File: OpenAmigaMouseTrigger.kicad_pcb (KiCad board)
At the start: 2 copper layers, 23.9 x 22.9 mm, 8 parts, among them J1 AMIGA_SIGNALS, J2 OUTPUT, J3 POWER, J99 OSHW_LOGO, U1 74LS74

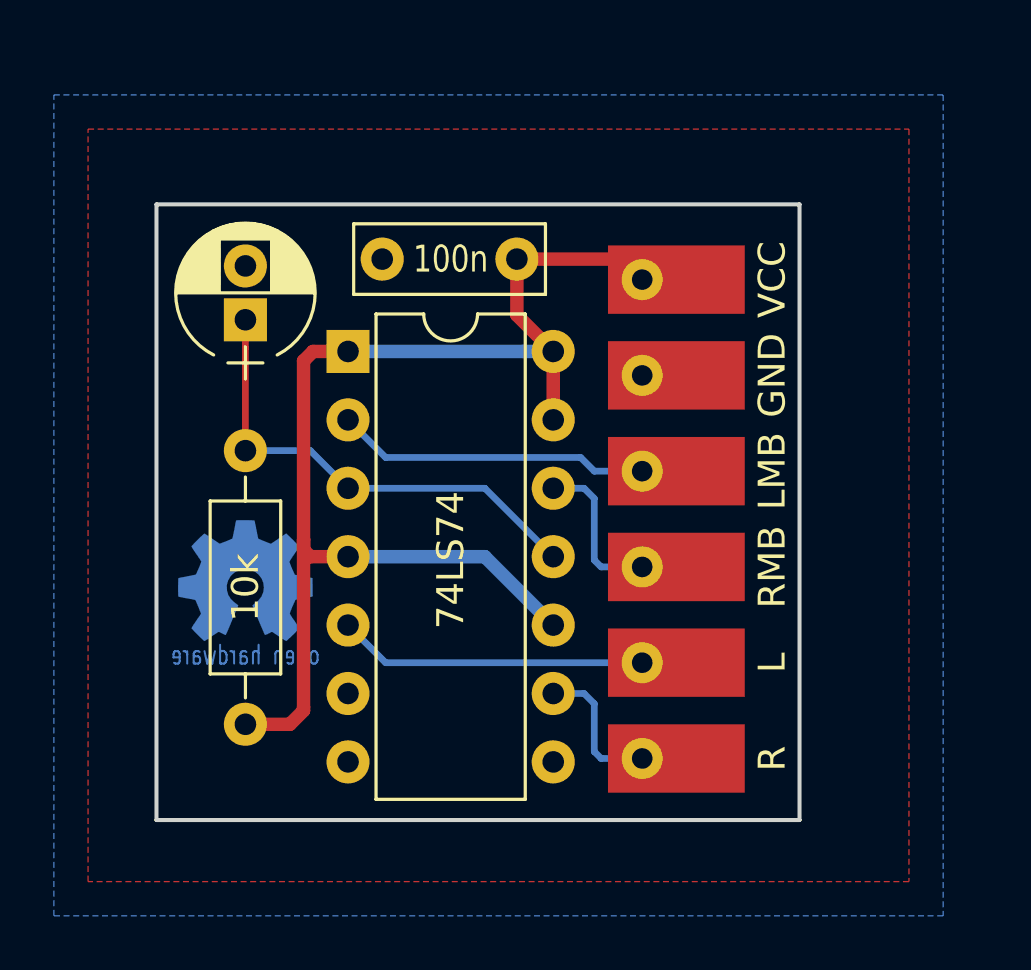
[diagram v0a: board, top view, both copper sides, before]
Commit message: Round corners, stitch grounds, routing adjustments
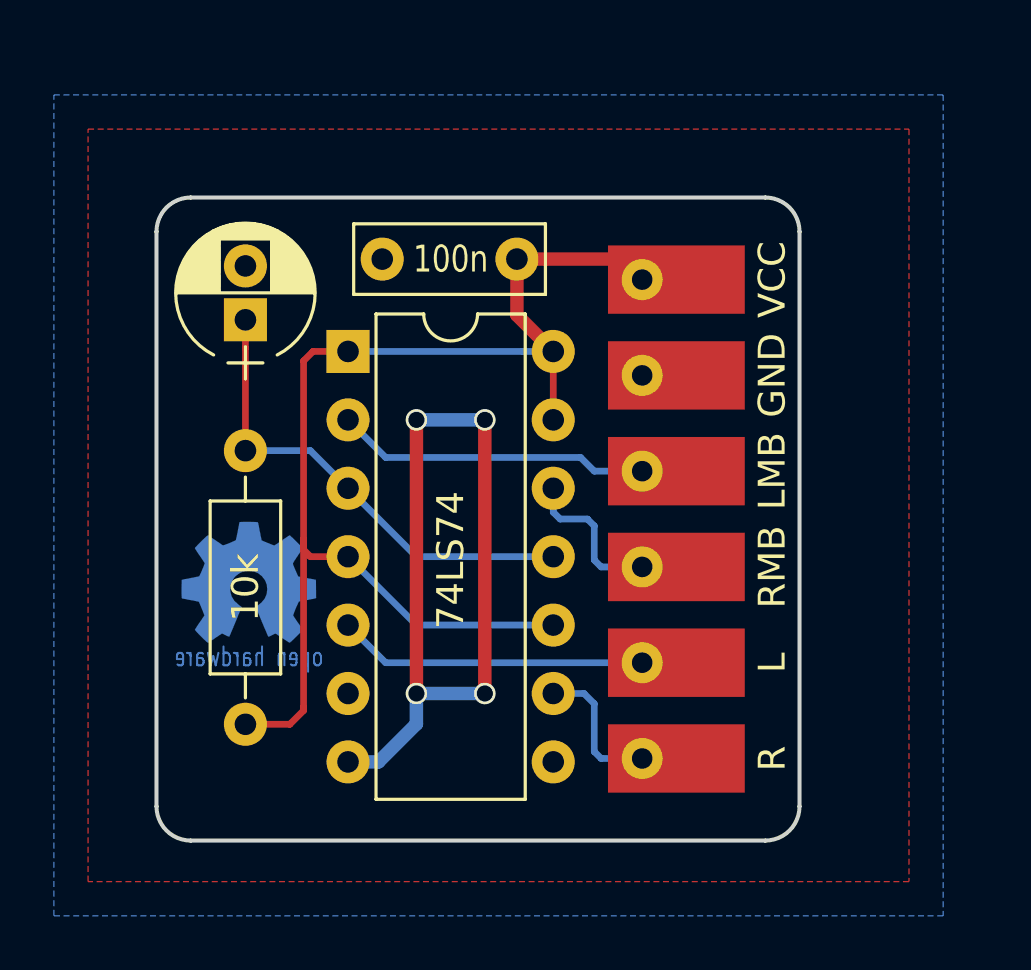
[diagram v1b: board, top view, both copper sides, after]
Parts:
- moved J99 0.14 mm to (126.6, 110.8)
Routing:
- net GND: track 0.00 -> 29.7 mm, vias 0 -> 4
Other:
- board size 23.9 x 22.9 mm -> 23.9 x 23.9 mm

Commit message: Final touches for V1
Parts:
- added R2: 22k, Resistors_THT:R_Axial_DIN0207_L6.3mm_D2.5mm_P10.16mm_Horizontal, F.Cu at (140.6, 95.6)
- added R3: 22k, Resistors_THT:R_Axial_DIN0207_L6.3mm_D2.5mm_P10.16mm_Horizontal, F.Cu at (140.6, 118.5)
- R1: value 10k -> 4.7k
- moved J99 9.13 mm to (134.0, 116.2)
- moved J3 3.12 mm to (145.3, 99.9)
- moved J1 3.12 mm to (145.3, 107.1)
- moved J2 3.12 mm to (145.3, 114.2)
- moved C1 1.42 mm to (126.2, 99.7)
- moved R1 1.42 mm to (126.2, 114.7)
- moved U1 1.42 mm to (130.0, 100.8)
- moved C2 1.42 mm to (136.3, 97.4)
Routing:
- net VCC: track 46.9 -> 66.3 mm
- net Net-(J1-Pad1): track 11.7 -> 14.9 mm
- net Net-(J2-Pad1): track 11.5 -> 14.5 mm
- net Net-(J2-Pad2): track 5.34 -> 8.06 mm
- net Net-(J1-Pad2): track 5.78 -> 8.27 mm
- net GND: track 29.7 -> 31.9 mm
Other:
- board size 23.9 x 23.9 mm -> 26.7 x 26.7 mm
- board text added: "V1"

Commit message: V2 is ready
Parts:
- added R4: 330k, Resistors_THT:R_Axial_DIN0207_L6.3mm_D2.5mm_P10.16mm_Horizontal, F.Cu at (124.0, 104.5)
- J1: value AMIGA_SIGNALS -> INPUT_SIGNALS
- moved J99 11.1 mm to (125.6, 109.0)
- moved R1 9.65 mm to (140.6, 105.3), turned to 90 degrees
- moved J1 7.11 mm to (145.3, 99.9)
- moved J3 7.11 mm to (145.3, 107.1)
- moved C1 0.76 mm to (125.5, 99.7)
- moved R3 0.76 mm to (127.0, 114.7)
- moved R2 0.51 mm to (140.6, 119.0)
- renumbered R2 to R1, R3 to R2, R1 to R3
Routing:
- net Net-(J1-Pad1): track 14.9 -> 28.8 mm
- net Net-(C1-Pad1): track 17.9 -> 23.3 mm
- net Net-(J1-Pad2): track 8.27 -> 12.7 mm
- net VCC: track 66.3 -> 67.9 mm
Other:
- board size 26.7 x 26.7 mm -> 28.2 x 28.2 mm
- board text added: "I1"
- board text added: "I2"
- board text added: "O1"
- board text added: "O2"
- board text added: "V2"
- board text removed: "L"
- board text removed: "LMB"
- board text removed: "R"
- board text removed: "RMB"
- board text removed: "V1"

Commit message: Fix silkscreen URL
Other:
- board text added: "github.com/SukkoPera/ OpenAmigaMouseTrigger"
- board text removed: "github.com/SukkoPera/ OpenKickstartSwitcher"
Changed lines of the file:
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@@
   (gr_arc (start 148.59 94.234) (end 148.59 92.964) (angle 90) (layer Edge.Cuts) (width 0.15))
   (gr_arc (start 122.936 94.234) (end 121.666 94.234) (angle 90) (layer Edge.Cuts) (width 0.15))
-  (gr_text "github.com/SukkoPera/\nOpenKickstartSwitcher" (at 147.066 106.553 90) (layer B.SilkS)
+  (gr_text "github.com/SukkoPera/\nOpenAmigaMouseTrigger" (at 147.066 106.553 90) (layer B.SilkS)
     (effects (font (size 1 1) (thickness 0.15)) (justify mirror))
   )
